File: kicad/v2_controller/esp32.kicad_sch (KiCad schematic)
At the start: 20 parts, among them J1 Conn_02x10_Odd_Even, J2 Conn_02x10_Odd_Even, J5 Conn_02x04_Odd_Even, Q1 S8050, Q2 S8050, SW18 SW_MEC_5E, SW19 SW_MEC_5E, U3 74AHCT1G125

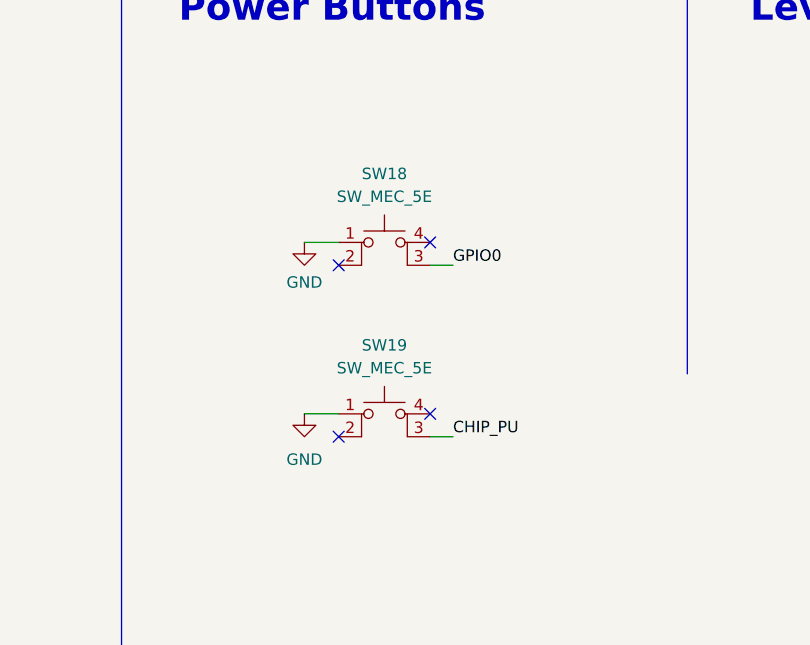
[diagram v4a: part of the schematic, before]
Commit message: [kicad] more v2 controller work
Update the switch symbols to single pole, since the XKB TS-1187A
footprint only uses 2 pins, even though it has 4 pads.

Also tweak the positioning of the ESP32-S3-WROOM and the board edge,
so that the antenna is off the board.
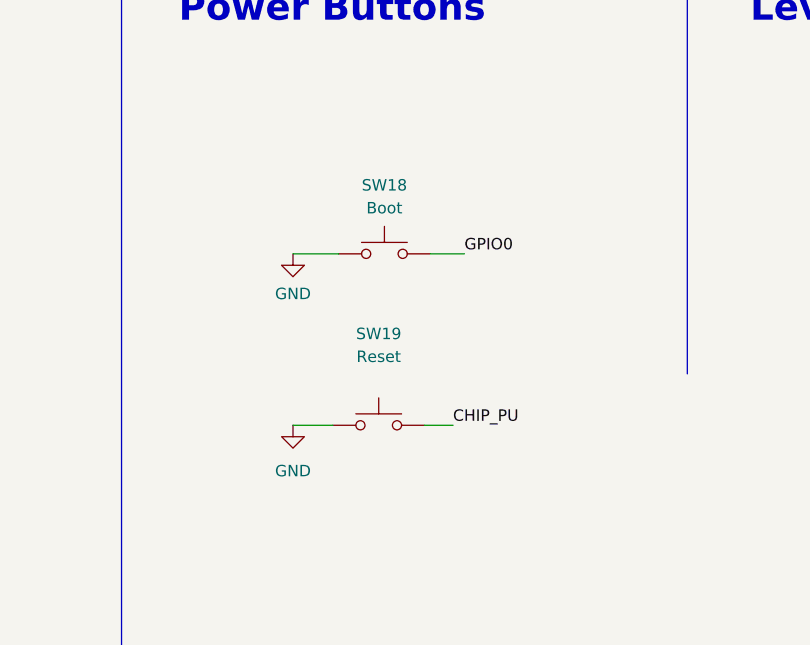
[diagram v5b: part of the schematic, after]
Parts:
- J5: footprint Connector_PinHeader_2.54mm:PinHeader_2x04_P2.54mm_Vertical -> Connector_PinSocket_2.54mm:PinSocket_2x04_P2.54mm_Vertical
- SW18: value SW_MEC_5E -> Boot; symbol Switch:SW_MEC_5E -> Switch:SW_Push
- SW19: value SW_MEC_5E -> Reset; symbol Switch:SW_MEC_5E -> Switch:SW_Push
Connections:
- net CHIP_PU: now also SW19.2; no longer SW19.3 (K)
- net GPIO0: now also SW18.2; no longer SW18.3 (K)
- no-connect marks 13 -> 9
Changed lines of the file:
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@@
   (no_connect (at 209.55 106.68))
   (no_connect (at 90.17 65.405))
-  (no_connect (at 138.43 153.67))
-  (no_connect (at 148.59 170.18))
-  (no_connect (at 138.43 172.72))
-  (no_connect (at 148.59 151.13))
   (no_connect (at 90.17 67.945))
   (no_connect (at 128.27 94.615))
@@
     (stroke (width 0) (type default))
   )
-  (wire (pts (xy 134.62 170.18) (xy 138.43 170.18))
-    (stroke (width 0) (type default))
-  )
   (wire (pts (xy 146.05 62.865) (xy 152.4 62.865))
     (stroke (width 0) (type default))
@@
     (stroke (width 0) (type default))
   )
-  (wire (pts (xy 134.62 151.13) (xy 138.43 151.13))
+  (wire (pts (xy 133.35 152.4) (xy 138.43 152.4))
     (stroke (width 0) (type default))
   )
@@
     (stroke (width 0) (type default))
   )
+  (wire (pts (xy 133.35 171.45) (xy 137.795 171.45))
+    (stroke (width 0) (type default))
+  )
   (wire (pts (xy 63.5 42.545) (xy 63.5 45.085))
     (stroke (width 0) (type default))
@@
     (stroke (width 0) (type default))
   )
-  (wire (pts (xy 148.59 153.67) (xy 151.13 153.67))
+  (wire (pts (xy 148.59 152.4) (xy 152.4 152.4))
     (stroke (width 0) (type default))
   )
@@
     (stroke (width 0) (type default))
   )
-  (wire (pts (xy 148.59 172.72) (xy 151.13 172.72))
+  (wire (pts (xy 147.955 171.45) (xy 151.13 171.45))
     (stroke (width 0) (type default))
   )
@@
     )
   )
-  (label "GPIO0" (at 151.13 153.67 0) (fields_autoplaced)
+  (label "GPIO0" (at 152.4 152.4 0) (fields_autoplaced)
     (effects (font (size 1.27 1.27)) (justify left bottom))
   )
@@
     )
   )
-  (label "CHIP_PU" (at 151.13 172.72 0) (fields_autoplaced)
+  (label "CHIP_PU" (at 151.13 171.45 0) (fields_autoplaced)
     (effects (font (size 1.27 1.27)) (justify left bottom))
   )
@@
       (effects (font (size 1.27 1.27)))
     )
-    (property "Footprint" "Connector_PinHeader_2.54mm:PinHeader_2x04_P2.54mm_Vertical" (at 259.08 86.36 0)
+    (property "Footprint" "Connector_PinSocket_2.54mm:PinSocket_2x04_P2.54mm_Vertical" (at 259.08 86.36 0)
       (effects (font (size 1.27 1.27)) hide)
     )
@@
     )
   )
-  (symbol (lib_id "Switch:SW_MEC_5E") (at 143.51 153.67 0) (unit 1)
-    (in_bom yes) (on_board yes) (dnp no) (fields_autoplaced)
-    (property "Reference" "SW18" (at 143.51 143.51 0)
-      (effects (font (size 1.27 1.27)))
-    )
-    (property "Value" "SW_MEC_5E" (at 143.51 146.05 0)
-      (effects (font (size 1.27 1.27)))
-    )
-    (property "Footprint" "Button_Switch_SMD:SW_Push_1P1T_XKB_TS-1187A" (at 143.51 146.05 0)
-      (effects (font (size 1.27 1.27)) hide)
-    )
-    (property "Datasheet" "http://www.apem.com/int/index.php?controller=attachment&id_attachment=1371" (at 143.51 146.05 0)
-      (effects (font (size 1.27 1.27)) hide)
-    )
-    (property "LCSC Part #" "C318884" (at 143.51 153.67 0)
-      (effects (font (size 1.27 1.27)) hide)
-    )
-    (property "Manufacturer Part #" "" (at 143.51 153.67 0)
+  (symbol (lib_id "Switch:SW_Push") (at 143.51 152.4 0) (unit 1)
+    (in_bom yes) (on_board yes) (dnp no) (fields_autoplaced)
+    (property "Reference" "SW18" (at 143.51 144.78 0)
+      (effects (font (size 1.27 1.27)))
+    )
+    (property "Value" "Boot" (at 143.51 147.32 0)
+      (effects (font (size 1.27 1.27)))
+    )
+    (property "Footprint" "Button_Switch_SMD:SW_Push_1P1T_XKB_TS-1187A" (at 143.51 147.32 0)
+      (effects (font (size 1.27 1.27)) hide)
+    )
+    (property "Datasheet" "~" (at 143.51 147.32 0)
+      (effects (font (size 1.27 1.27)) hide)
+    )
+    (property "LCSC Part #" "C318884" (at 143.51 152.4 0)
+      (effects (font (size 1.27 1.27)) hide)
+    )
+    (property "Manufacturer Part #" "" (at 143.51 152.4 0)
       (effects (font (size 1.27 1.27)) hide)
     )
     (pin "1")
     (pin "2")
-    (pin "3")
-    (pin "4")
     (instances
       (project "v2_controller"
@@
     )
   )
-  (symbol (lib_id "power:GND") (at 134.62 151.13 0) (unit 1)
-    (in_bom yes) (on_board yes) (dnp no) (fields_autoplaced)
-    (property "Reference" "#PWR028" (at 134.62 157.48 0)
-      (effects (font (size 1.27 1.27)) hide)
-    )
-    (property "Value" "GND" (at 134.62 155.575 0)
-      (effects (font (size 1.27 1.27)))
-    )
-    (property "Footprint" "" (at 134.62 151.13 0)
-      (effects (font (size 1.27 1.27)) hide)
-    )
-    (property "Datasheet" "" (at 134.62 151.13 0)
+  (symbol (lib_id "power:GND") (at 133.35 152.4 0) (unit 1)
+    (in_bom yes) (on_board yes) (dnp no) (fields_autoplaced)
+    (property "Reference" "#PWR028" (at 133.35 158.75 0)
+      (effects (font (size 1.27 1.27)) hide)
+    )
+    (property "Value" "GND" (at 133.35 156.845 0)
+      (effects (font (size 1.27 1.27)))
+    )
+    (property "Footprint" "" (at 133.35 152.4 0)
+      (effects (font (size 1.27 1.27)) hide)
+    )
+    (property "Datasheet" "" (at 133.35 152.4 0)
       (effects (font (size 1.27 1.27)) hide)
     )
@@
     )
   )
-  (symbol (lib_id "power:GND") (at 134.62 170.18 0) (unit 1)
-    (in_bom yes) (on_board yes) (dnp no) (fields_autoplaced)
-    (property "Reference" "#PWR029" (at 134.62 176.53 0)
-      (effects (font (size 1.27 1.27)) hide)
-    )
-    (property "Value" "GND" (at 134.62 175.26 0)
-      (effects (font (size 1.27 1.27)))
-    )
-    (property "Footprint" "" (at 134.62 170.18 0)
-      (effects (font (size 1.27 1.27)) hide)
-    )
-    (property "Datasheet" "" (at 134.62 170.18 0)
+  (symbol (lib_id "power:GND") (at 133.35 171.45 0) (unit 1)
+    (in_bom yes) (on_board yes) (dnp no) (fields_autoplaced)
+    (property "Reference" "#PWR029" (at 133.35 177.8 0)
+      (effects (font (size 1.27 1.27)) hide)
+    )
+    (property "Value" "GND" (at 133.35 176.53 0)
+      (effects (font (size 1.27 1.27)))
+    )
+    (property "Footprint" "" (at 133.35 171.45 0)
+      (effects (font (size 1.27 1.27)) hide)
+    )
+    (property "Datasheet" "" (at 133.35 171.45 0)
       (effects (font (size 1.27 1.27)) hide)
     )
@@
     )
   )
-  (symbol (lib_id "Switch:SW_MEC_5E") (at 143.51 172.72 0) (unit 1)
-    (in_bom yes) (on_board yes) (dnp no) (fields_autoplaced)
-    (property "Reference" "SW19" (at 143.51 162.56 0)
-      (effects (font (size 1.27 1.27)))
-    )
-    (property "Value" "SW_MEC_5E" (at 143.51 165.1 0)
-      (effects (font (size 1.27 1.27)))
-    )
-    (property "Footprint" "Button_Switch_SMD:SW_Push_1P1T_XKB_TS-1187A" (at 143.51 165.1 0)
-      (effects (font (size 1.27 1.27)) hide)
-    )
-    (property "Datasheet" "http://www.apem.com/int/index.php?controller=attachment&id_attachment=1371" (at 143.51 165.1 0)
-      (effects (font (size 1.27 1.27)) hide)
-    )
-    (property "LCSC Part #" "C318884" (at 143.51 172.72 0)
-      (effects (font (size 1.27 1.27)) hide)
-    )
-    (property "Manufacturer Part #" "" (at 143.51 172.72 0)
+  (symbol (lib_id "Switch:SW_Push") (at 142.875 171.45 0) (unit 1)
+    (in_bom yes) (on_board yes) (dnp no) (fields_autoplaced)
+    (property "Reference" "SW19" (at 142.875 161.29 0)
+      (effects (font (size 1.27 1.27)))
+    )
+    (property "Value" "Reset" (at 142.875 163.83 0)
+      (effects (font (size 1.27 1.27)))
+    )
+    (property "Footprint" "Button_Switch_SMD:SW_Push_1P1T_XKB_TS-1187A" (at 142.875 166.37 0)
+      (effects (font (size 1.27 1.27)) hide)
+    )
+    (property "Datasheet" "~" (at 142.875 166.37 0)
+      (effects (font (size 1.27 1.27)) hide)
+    )
+    (property "LCSC Part #" "C318884" (at 142.875 171.45 0)
+      (effects (font (size 1.27 1.27)) hide)
+    )
+    (property "Manufacturer Part #" "" (at 142.875 171.45 0)
       (effects (font (size 1.27 1.27)) hide)
     )
     (pin "1")
     (pin "2")
-    (pin "3")
-    (pin "4")
-    (instances
-      (project "v2_controller"
+    (instances
+      (project "v2_controller"

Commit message: [kicad] finish initial component placement
This will probably need to be tweaked further once I begin routing,
but is a start for now.
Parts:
- added J6: Conn_02x03_Odd_Even, Connector_PinSocket_2.54mm:PinSocket_2x03_P2.54mm_Vertical, symbol Connector_Generic:Conn_02x03_Odd_Even
- renumbered J1 to J3, J2 to J4, R4 to R2, R5 to R3
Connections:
- net ROW0: now also J6.2 (Pin_2)
- net ROW1: now also J6.3 (Pin_3)
- net ROW2: now also J6.4 (Pin_4)
- net ROW3: now also J6.5 (Pin_5)
- net ROW4: now also J6.6 (Pin_6)
- net COL10: now reaches U?.25 (GPIO48/SPICLK_N)
- net COL10: now also J6.1 (Pin_1)
- no-connect marks 9 -> 8
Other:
- note added: "Hat Switch"
- moved on the sheet: J5

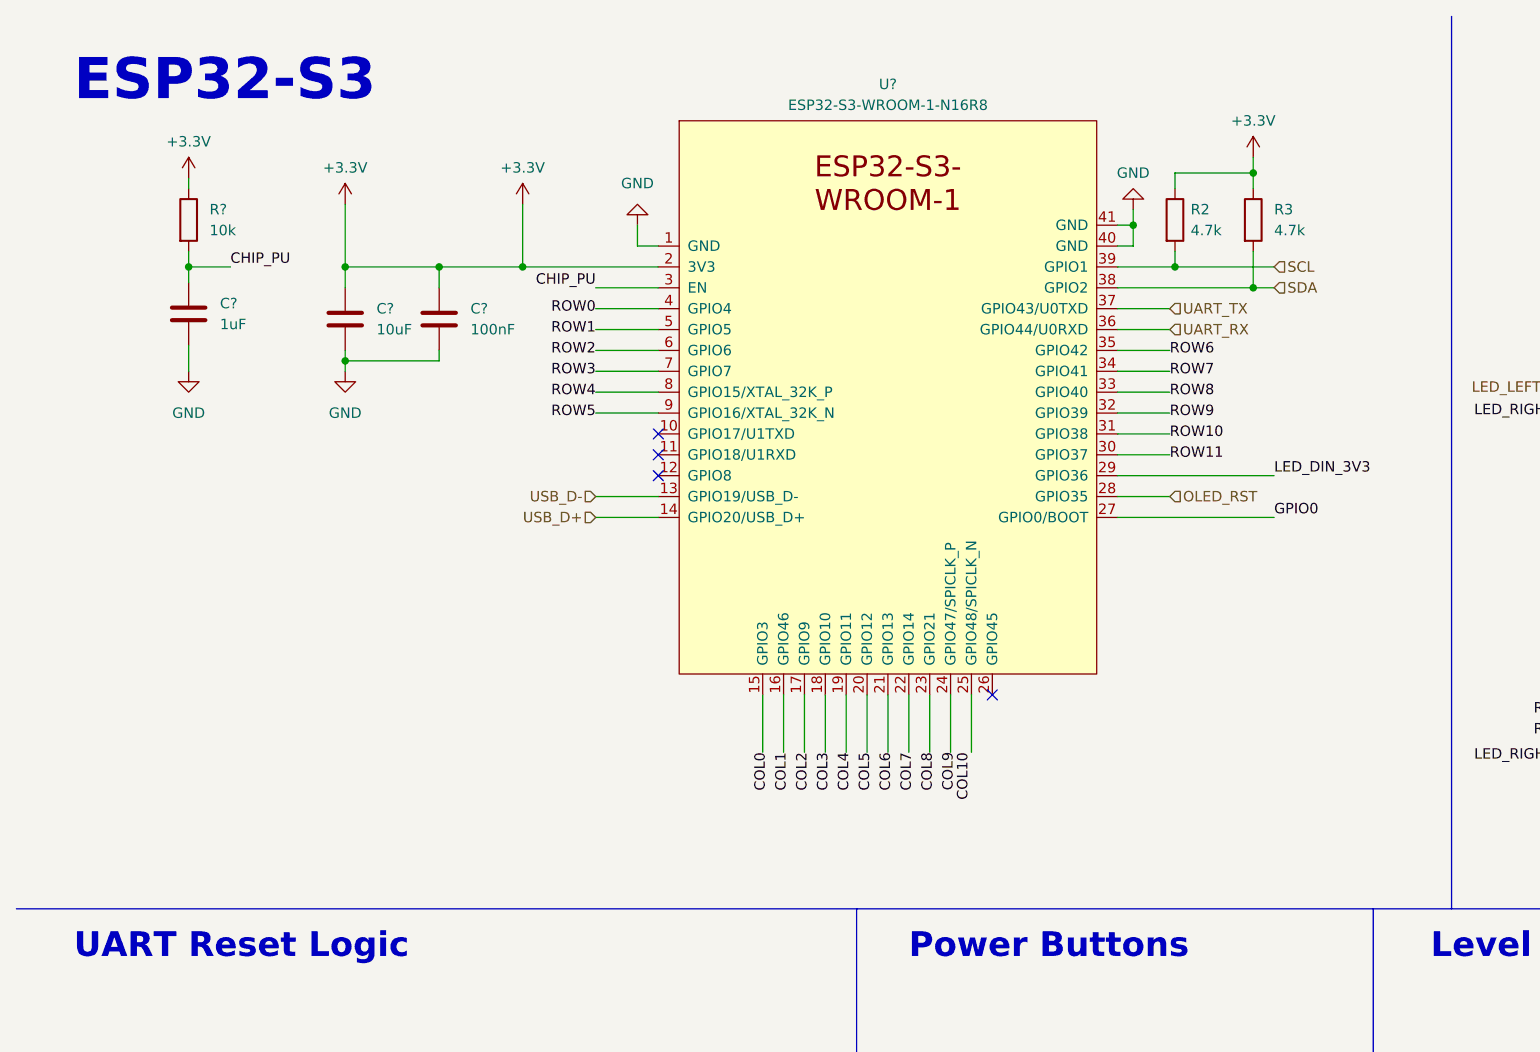
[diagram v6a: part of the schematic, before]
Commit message: [kicad] begin routing some traces
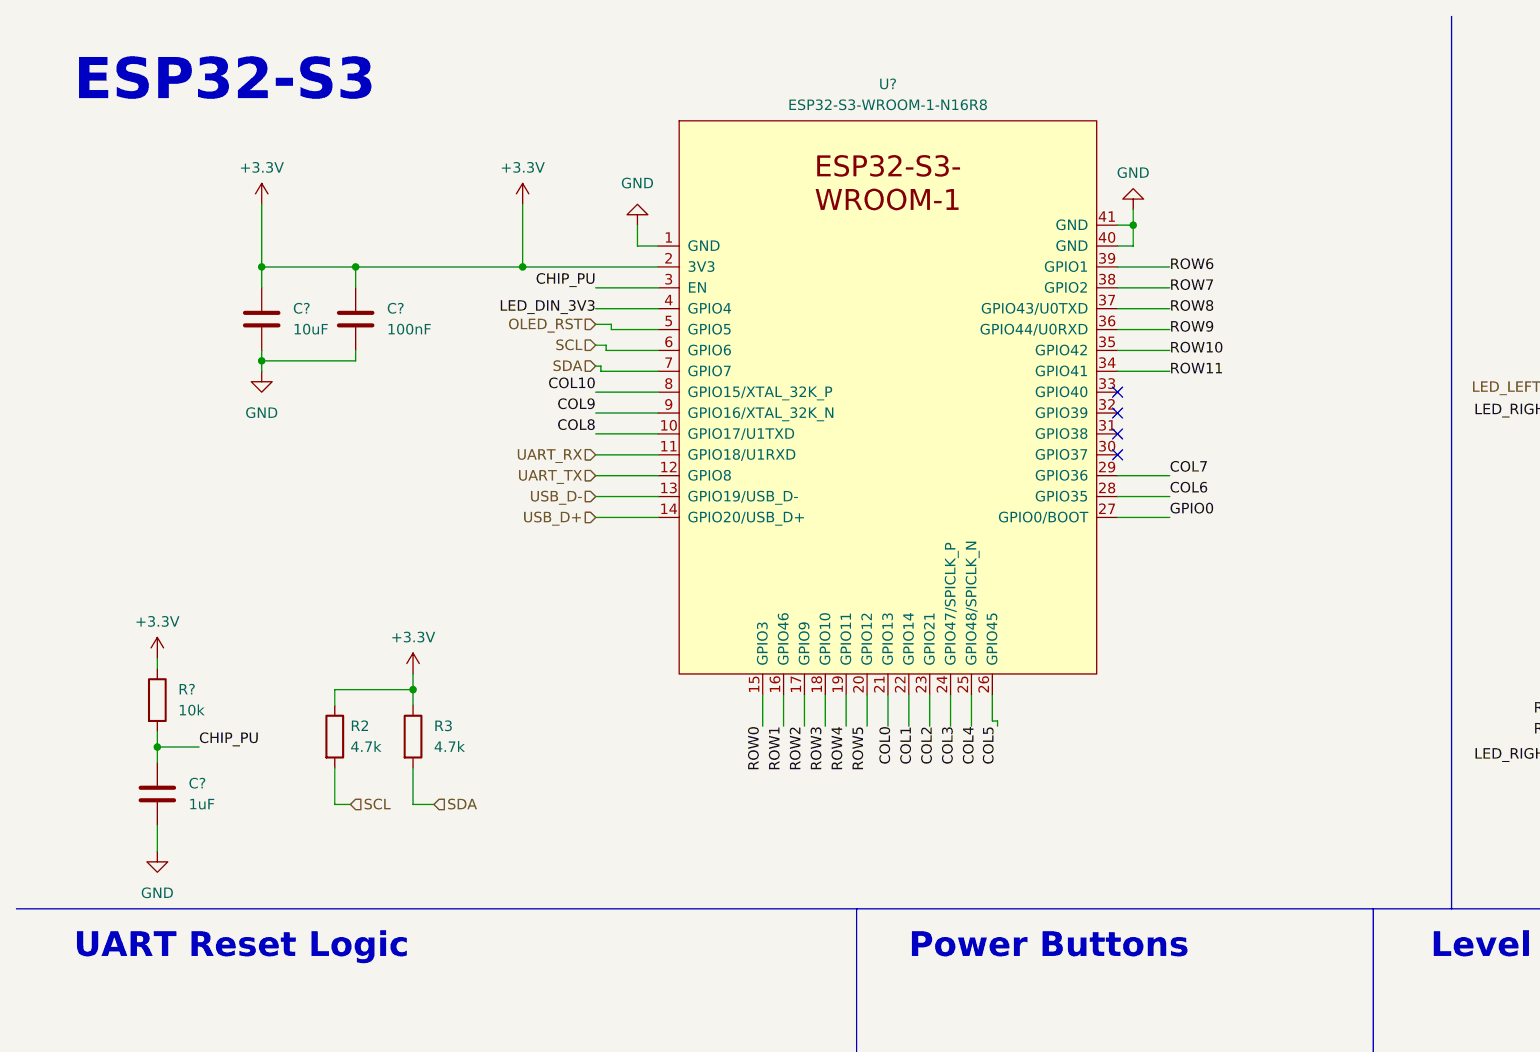
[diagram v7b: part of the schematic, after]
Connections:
- net COL0: now also U?.21 (GPIO13); no longer U?.15 (GPIO3)
- net COL1: now also U?.22 (GPIO14); no longer U?.16 (GPIO46)
- net COL10: now also U?.8 (GPIO15/XTAL_32K_P); no longer U?.25 (GPIO48/SPICLK_N)
- net COL2: now also U?.23 (GPIO21); no longer U?.17 (GPIO9)
- net COL3: now also U?.24 (GPIO47/SPICLK_P); no longer U?.18 (GPIO10)
- net COL4: now also U?.25 (GPIO48/SPICLK_N); no longer U?.19 (GPIO11)
- net COL5: now also U?.26 (GPIO45); no longer U?.20 (GPIO12)
- net COL6: now also U?.28 (GPIO35); no longer U?.21 (GPIO13)
- net COL7: now also U?.29 (GPIO36); no longer U?.22 (GPIO14)
- net COL8: now also U?.10 (GPIO17/U1TXD); no longer U?.23 (GPIO21)
- net COL9: now also U?.9 (GPIO16/XTAL_32K_N); no longer U?.24 (GPIO47/SPICLK_P)
- net LED_DIN_3V3: now also U?.4 (GPIO4); no longer U?.29 (GPIO36)
- net OLED_RST: now also U?.5 (GPIO5); no longer U?.28 (GPIO35)
- net ROW0: now also U?.15 (GPIO3); no longer U?.4 (GPIO4)
- net ROW1: now also U?.16 (GPIO46); no longer U?.5 (GPIO5)
- net ROW10: now also U?.35 (GPIO42); no longer U?.31 (GPIO38)
- net ROW11: now also U?.34 (GPIO41); no longer U?.30 (GPIO37)
- net ROW2: now also U?.17 (GPIO9); no longer U?.6 (GPIO6)
- net ROW3: now also U?.18 (GPIO10); no longer U?.7 (GPIO7)
- net ROW4: now also U?.19 (GPIO11); no longer U?.8 (GPIO15/XTAL_32K_P)
- net ROW5: now also U?.20 (GPIO12); no longer U?.9 (GPIO16/XTAL_32K_N)
- net ROW6: now also U?.39 (GPIO1); no longer U?.35 (GPIO42)
- net ROW7: now also U?.38 (GPIO2); no longer U?.34 (GPIO41)
- net ROW8: now also U?.37 (GPIO43/U0TXD); no longer U?.33 (GPIO40)
- net ROW9: now also U?.36 (GPIO44/U0RXD); no longer U?.32 (GPIO39)
- net SCL: now also U?.6 (GPIO6); no longer U?.39 (GPIO1)
- net SDA: now also U?.7 (GPIO7); no longer U?.38 (GPIO2)
- net UART_RX: now also U?.11 (GPIO18/U1RXD); no longer U?.36 (GPIO44/U0RXD)
- net UART_TX: now also U?.12 (GPIO8); no longer U?.37 (GPIO43/U0TXD)
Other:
- moved on the sheet: C?, R2, R3, R?
